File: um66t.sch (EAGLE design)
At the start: 12 parts, among them IC1 7833, T1 BC547

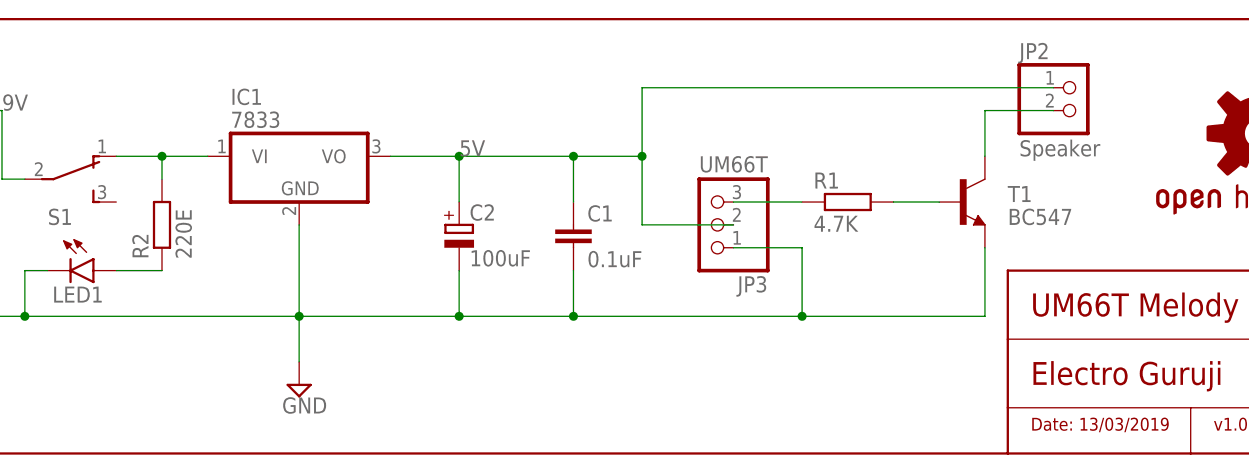
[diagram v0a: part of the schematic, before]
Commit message: Replaced 7833 with 10E resistor
Changed BC547 Package
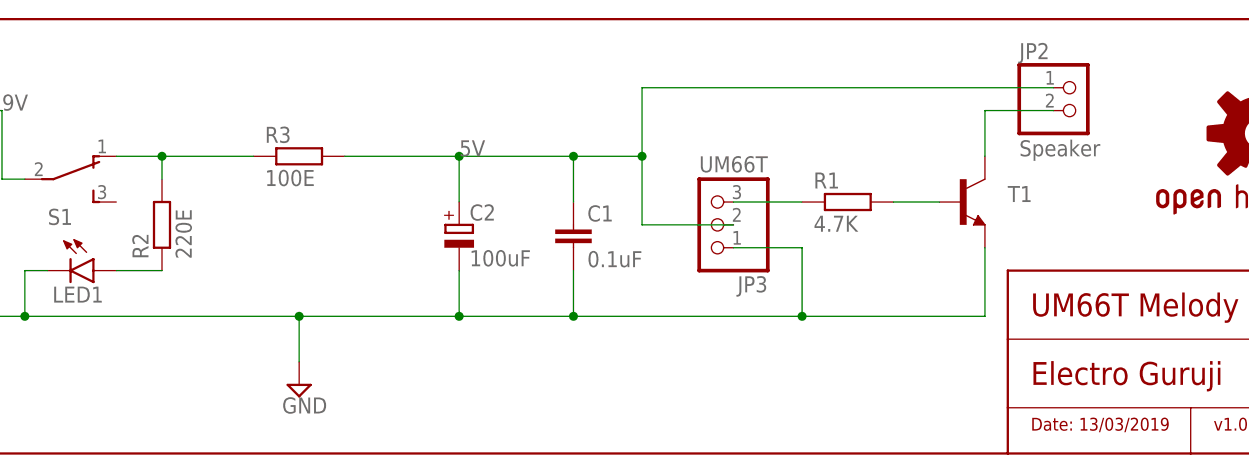
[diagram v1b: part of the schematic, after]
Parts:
- removed IC1: 7833, linear:7805TV
- added R3: 100E, resistor:R-EU_0204/5
- T1: value BC547 -> (none); device transistor:BC547 -> transistor:BC237-NPN-TO92-CBE
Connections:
- net 5V: now also R3.2; no longer IC1.VO
- net GND: no longer IC1.GND
- net N$2: now also R3.1; no longer IC1.VI
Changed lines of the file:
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@@
 <part name="C2" library="resistor" library_urn="urn:adsk.eagle:library:348" deviceset="CPOL-EU" device="E5-5" package3d_urn="urn:adsk.eagle:package:23367/2" value="100uF"/>
 <part name="R1" library="resistor" library_urn="urn:adsk.eagle:library:348" deviceset="R-EU_" device="0204/5" package3d_urn="urn:adsk.eagle:package:23488/1" value="4.7K"/>
-<part name="T1" library="transistor" library_urn="urn:adsk.eagle:library:402" deviceset="BC547" device="" package3d_urn="urn:adsk.eagle:package:28523/2"/>
-<part name="IC1" library="linear" library_urn="urn:adsk.eagle:library:262" deviceset="78*" device="TV" package3d_urn="urn:adsk.eagle:package:16417/2" technology="05" value="7833"/>
+<part name="T1" library="transistor" library_urn="urn:adsk.eagle:library:402" deviceset="*-NPN-" device="TO92-CBE" package3d_urn="urn:adsk.eagle:package:29921/2" technology="BC237"/>
 <part name="SUPPLY1" library="supply2" library_urn="urn:adsk.eagle:library:372" deviceset="GND" device=""/>
 <part name="R2" library="resistor" library_urn="urn:adsk.eagle:library:348" deviceset="R-EU_" device="0204/5" package3d_urn="urn:adsk.eagle:package:23488/1" value="220E"/>
 <part name="LED1" library="led" library_urn="urn:adsk.eagle:library:259" deviceset="LED" device="5MM" package3d_urn="urn:adsk.eagle:package:15799/2"/>
 <part name="LOGO1" library="SparkFun-Aesthetics" library_urn="urn:adsk.eagle:library:507" deviceset="OSHW-LOGO" device="M-COPPER"/>
+<part name="R3" library="resistor" library_urn="urn:adsk.eagle:library:348" deviceset="R-EU_" device="0204/5" package3d_urn="urn:adsk.eagle:package:23488/1" value="100E"/>
 </parts>
 <sheets>
@@
 <attribute name="VALUE" x="88.9" y="60.96" size="1.778" layer="96"/>
 </instance>
-<instance part="IC1" gate="A1" x="10.16" y="68.58" smashed="yes">
-<attribute name="NAME" x="2.54" y="74.295" size="1.778" layer="95"/>
-<attribute name="VALUE" x="2.54" y="71.755" size="1.778" layer="96"/>
-</instance>
 <instance part="SUPPLY1" gate="GND" x="10.16" y="43.18" smashed="yes">
 <attribute name="VALUE" x="8.255" y="40.005" size="1.778" layer="96"/>
@@
 </instance>
 <instance part="LOGO1" gate="G$1" x="116.84" y="71.12" smashed="yes"/>
+<instance part="R3" gate="G$1" x="10.16" y="68.58" smashed="yes">
+<attribute name="NAME" x="6.35" y="70.0786" size="1.778" layer="95"/>
+<attribute name="VALUE" x="6.35" y="65.278" size="1.778" layer="96"/>
+</instance>
 </instances>
 <busses>
@@
 <segment>
 <pinref part="S1" gate="BEF1" pin="O"/>
-<pinref part="IC1" gate="A1" pin="VI"/>
 <wire x1="-10.16" y1="68.58" x2="-5.08" y2="68.58" width="0.1524" layer="91"/>
 <pinref part="R2" gate="G$1" pin="2"/>
-<wire x1="-5.08" y1="68.58" x2="0" y2="68.58" width="0.1524" layer="91"/>
 <wire x1="-5.08" y1="66.04" x2="-5.08" y2="68.58" width="0.1524" layer="91"/>
 <junction x="-5.08" y="68.58"/>
+<pinref part="R3" gate="G$1" pin="1"/>
+<wire x1="5.08" y1="68.58" x2="-5.08" y2="68.58" width="0.1524" layer="91"/>
 </segment>
 </net>
 <net name="5V" class="0">
 <segment>
-<pinref part="IC1" gate="A1" pin="VO"/>
-<wire x1="20.32" y1="68.58" x2="27.94" y2="68.58" width="0.1524" layer="91"/>
+<wire x1="15.24" y1="68.58" x2="27.94" y2="68.58" width="0.1524" layer="91"/>
 <pinref part="C2" gate="G$1" pin="+"/>
 <wire x1="27.94" y1="68.58" x2="27.94" y2="63.5" width="0.1524" layer="91"/>
@@
 <junction x="48.26" y="68.58"/>
 <label x="27.94" y="68.58" size="1.778" layer="95"/>
+<pinref part="R3" gate="G$1" pin="2"/>
 </segment>
 </net>
@@
 <pinref part="JP1" gate="G$1" pin="2"/>
 <wire x1="-43.18" y1="63.5" x2="-33.02" y2="63.5" width="0.1524" layer="91"/>
-<pinref part="IC1" gate="A1" pin="GND"/>
-<wire x1="10.16" y1="60.96" x2="10.16" y2="50.8" width="0.1524" layer="91"/>
 <junction x="10.16" y="50.8"/>
 <pinref part="C2" gate="G$1" pin="-"/>

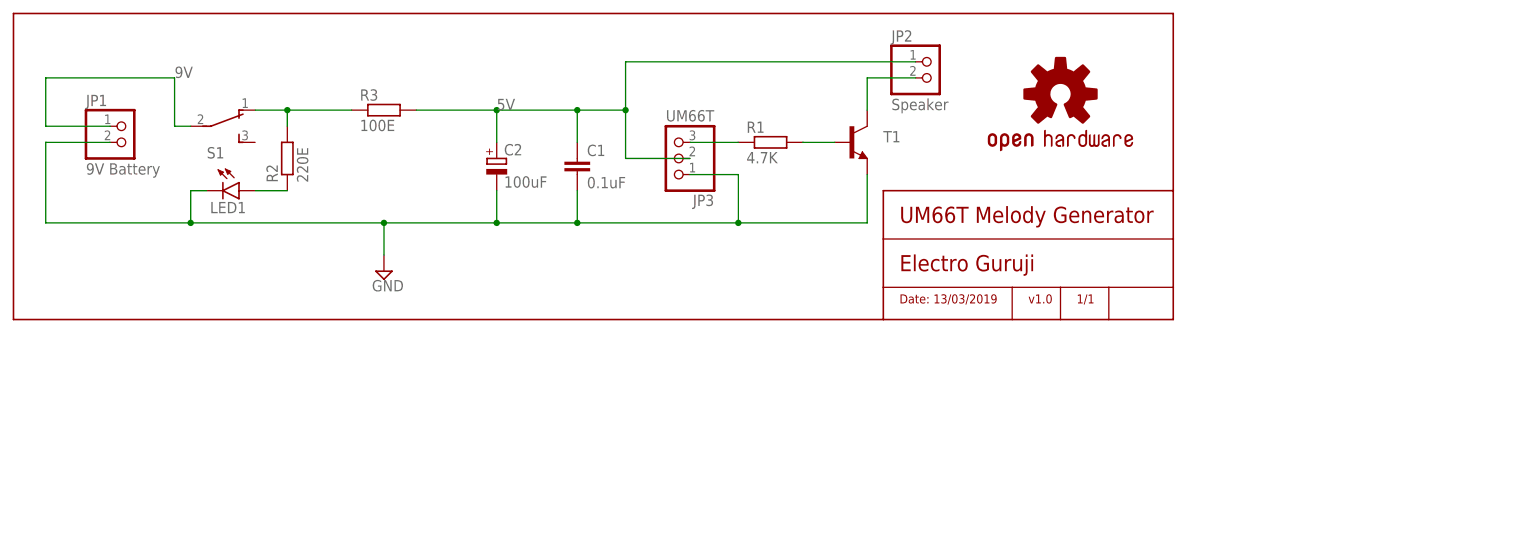
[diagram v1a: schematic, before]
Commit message: Changed 9V Battery to 5V Supply
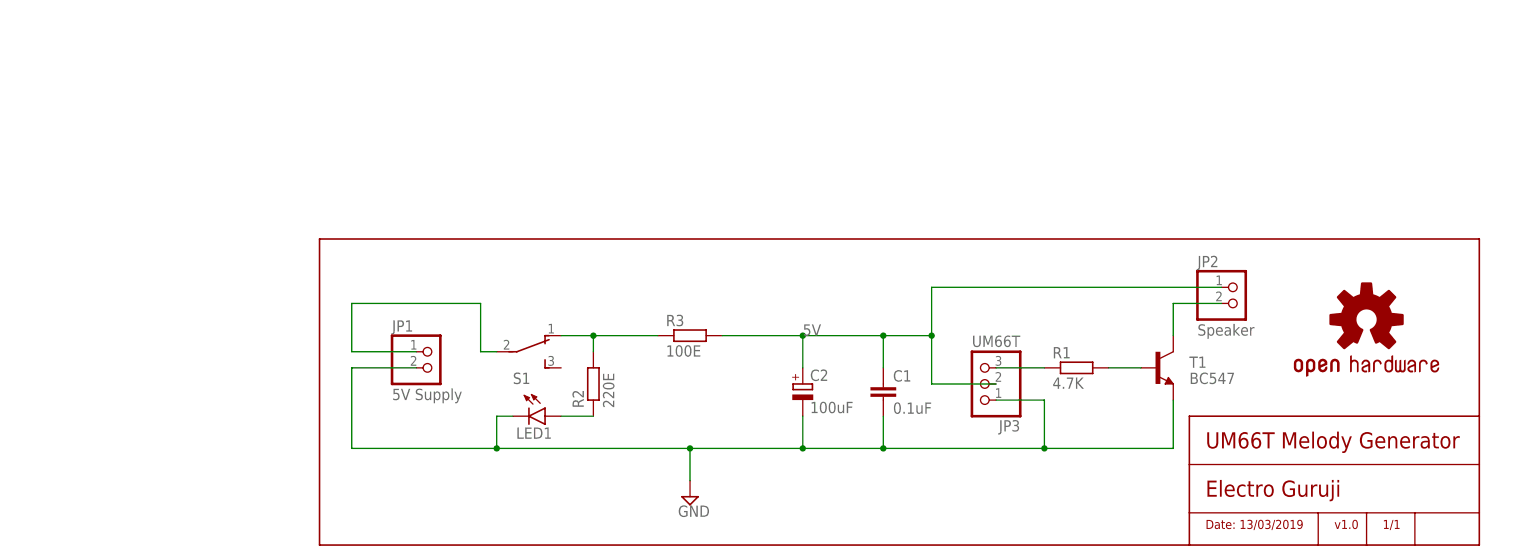
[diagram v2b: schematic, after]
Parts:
- JP1: value 9V Battery -> 5V Supply
- T1: value (none) -> BC547
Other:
- moved on the sheet: C1, C2, JP1, JP2, JP3, LED1, R1, R2, R3, S1, T1
